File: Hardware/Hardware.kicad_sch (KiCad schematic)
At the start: 0 parts

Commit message: feat: add symbols, footprints and 3d models
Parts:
- added U1: ESP32-C3_SUPERMINI_TH, footprints:MODULE_ESP32-C3_SUPERMINI_TH, symbol ESP32-C3_SUPERMINI_TH:ESP32-C3_SUPERMINI_TH
- added U2: DM-OLED096-636, DM-OLED096-636:MODULE_DM-OLED096-636, symbol DM-OLED096-636:DM-OLED096-636

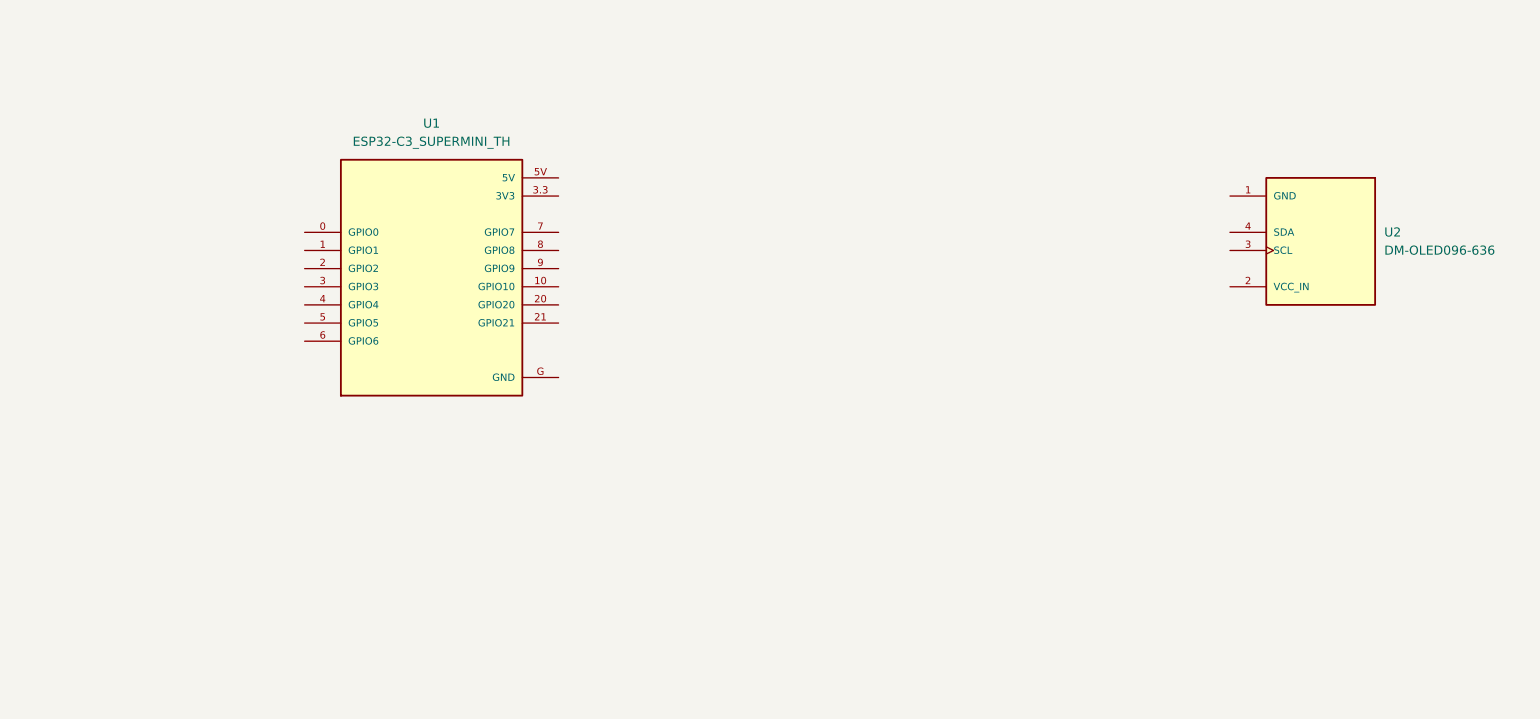
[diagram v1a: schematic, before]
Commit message: feat: add schematic design
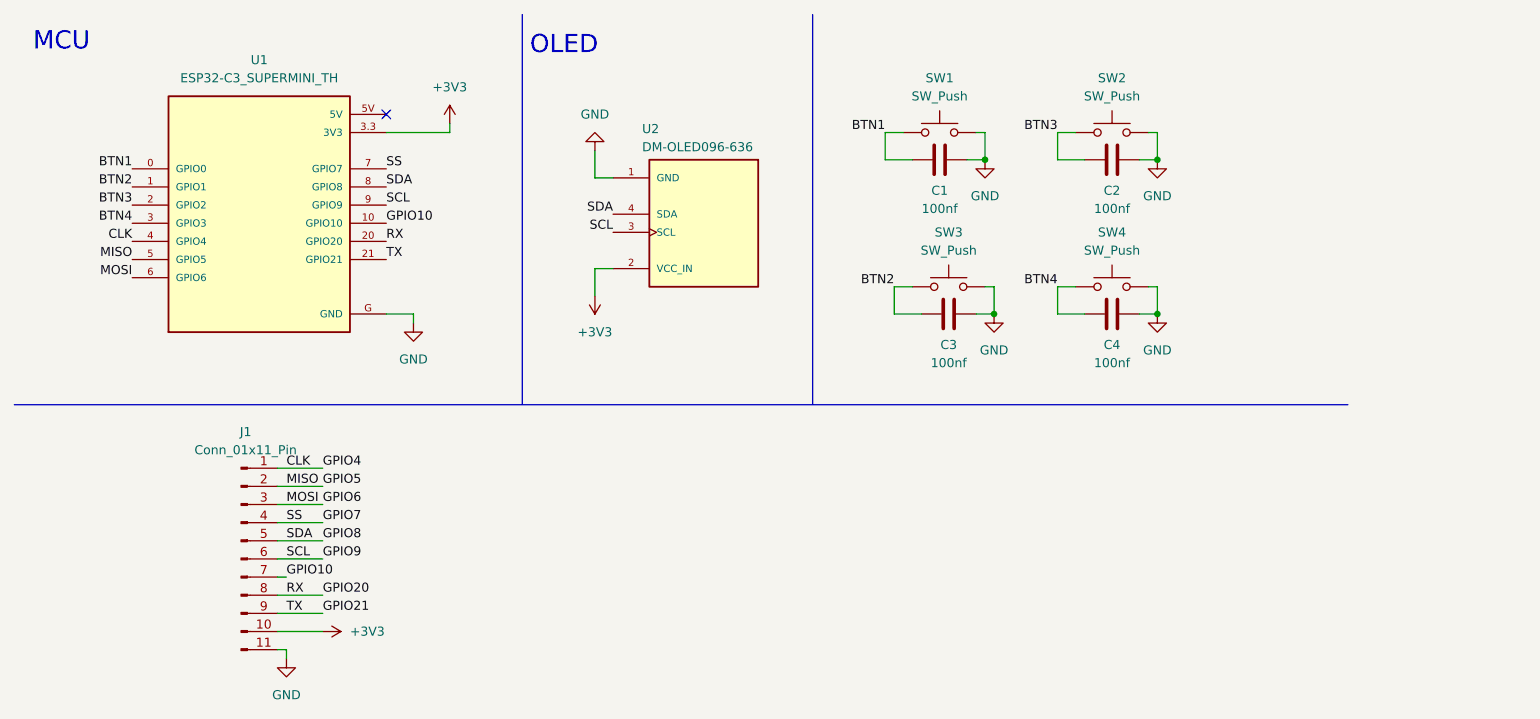
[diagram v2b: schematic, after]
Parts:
- added C1, C2, C3, C4: 100nf, symbol Device:C
- added J1: Conn_01x11_Pin, symbol Connector:Conn_01x11_Pin
- added SW1, SW2, SW3, SW4: SW_Push, symbol Switch:SW_Push
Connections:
- net BTN1: now reaches U1.0 (GPIO0)
- net BTN1: now also C1.1, SW1.1
- net BTN2: now reaches U1.1 (GPIO1)
- net BTN2: now also C3.1, SW3.1
- net GPIO10: now reaches U1.10 (GPIO10)
- net GPIO10: now also J1.7 (Pin_7)
- net BTN3: now reaches U1.2 (GPIO2)
- net BTN3: now also C2.1, SW2.1
- net GPIO20: now reaches U1.20 (GPIO20)
- net GPIO20: now also J1.8 (Pin_8)
- net GPIO21: now reaches U1.21 (GPIO21)
- net GPIO21: now also J1.9 (Pin_9)
- net BTN4: now reaches U1.3 (GPIO3)
- net BTN4: now also C4.1, SW4.1
- net +3V3: now reaches U1.3.3 (3V3)
- net +3V3: now also U2.2 (VCC_IN), J1.10 (Pin_10)
- net CLK: now reaches U1.4 (GPIO4)
- net CLK: now also J1.1 (Pin_1)
- net GPIO5: now reaches U1.5 (GPIO5)
- net GPIO5: now also J1.2 (Pin_2)
- net GPIO6: now reaches U1.6 (GPIO6)
- net GPIO6: now also J1.3 (Pin_3)
- net GPIO7: now reaches U1.7 (GPIO7)
- net GPIO7: now also J1.4 (Pin_4)
- net GPIO8: now reaches U1.8 (GPIO8)
- net GPIO8: now also U2.4 (SDA), J1.5 (Pin_5)
- net GPIO9: now reaches U1.9 (GPIO9)
- net GPIO9: now also U2.3 (SCL), J1.6 (Pin_6)
- net GND: now reaches U1.G (GND)
- net GND: now also U2.1 (GND), C1.2, C2.2, C3.2, C4.2, J1.11 (Pin_11), SW1.2, SW2.2, SW3.2, SW4.2
- no-connect marks 0 -> 1
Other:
- note added: "MCU"
- note added: "OLED"
- title: (none) -> My Esp32c3 
- moved on the sheet: U1, U2

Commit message: feat: change esp model & add footprints
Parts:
- J1: footprint (none) -> Connector_PinHeader_2.54mm:PinHeader_1x11_P2.54mm_Vertical
- SW1, SW2, SW3, SW4: footprint (none) -> Button_Switch_THT:SW_PUSH_6mm
- U1: footprint footprints:MODULE_ESP32-C3_SUPERMINI_TH -> footprints:MODULE_ESP32-C3_SUPERMINI
- U2: footprint DM-OLED096-636:MODULE_DM-OLED096-636 -> footprints:MODULE_DM-OLED096-636
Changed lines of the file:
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@@
 			)
 		)
-		(property "Footprint" ""
+		(property "Footprint" "Connector_PinHeader_2.54mm:PinHeader_1x11_P2.54mm_Vertical"
 			(at 43.18 87.63 0)
 			(effects
@@
 			)
 		)
-		(property "Footprint" ""
+		(property "Footprint" "Button_Switch_THT:SW_PUSH_6mm"
 			(at 140.97 22.86 0)
 			(effects
@@
 			)
 		)
-		(property "Footprint" "footprints:MODULE_ESP32-C3_SUPERMINI_TH"
+		(property "Footprint" "footprints:MODULE_ESP32-C3_SUPERMINI"
 			(at 45.72 38.1 0)
 			(effects
@@
 			)
 		)
-		(property "Footprint" ""
+		(property "Footprint" "Button_Switch_THT:SW_PUSH_6mm"
 			(at 165.1 44.45 0)
 			(effects
@@
 			)
 		)
-		(property "Footprint" ""
+		(property "Footprint" "Button_Switch_THT:SW_PUSH_6mm"
 			(at 142.24 44.45 0)
 			(effects
@@
 			)
 		)
-		(property "Footprint" "DM-OLED096-636:MODULE_DM-OLED096-636"
+		(property "Footprint" "footprints:MODULE_DM-OLED096-636"
 			(at 107.95 39.37 0)
 			(effects
@@
 			)
 		)
-		(property "Footprint" ""
+		(property "Footprint" "Button_Switch_THT:SW_PUSH_6mm"
 			(at 165.1 22.86 0)
 			(effects

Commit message: feat: add routes
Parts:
- removed J1: Conn_01x11_Pin, Connector_PinHeader_2.54mm:PinHeader_1x11_P2.54mm_Vertical, symbol Connector:Conn_01x11_Pin
- removed SW1, SW2, SW3, SW4: SW_Push, Button_Switch_THT:SW_PUSH_6mm, symbol Switch:SW_Push
- added C5: 100nF, Capacitor_SMD:C_0603_1608Metric_Pad1.08x0.95mm_HandSolder, symbol Device:C
- added J1: Conn_01x10_Socket, Connector_PinHeader_2.54mm:PinHeader_1x10_P2.54mm_Vertical, symbol Connector:Conn_01x10_Socket
- added S1: JS1400AFQ, footprints:SW_JS1400AFQ, symbol JS1400AFQ:JS1400AFQ
- C1, C2, C3, C4: value 100nf -> 100nF; footprint (none) -> Capacitor_SMD:C_0603_1608Metric_Pad1.08x0.95mm_HandSolder
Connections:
- net +3V3: now also J1.9 (Pin_9)
- net CLK: now also J1.1 (Pin_1)
- net GND: now also C5.2, J1.10 (Pin_10), S1.5, S1.G1 (GND), S1.G2 (GND)
- net BTN1 renamed F1
- net F1: now also C2.1, S1.3; no longer C1.1
- net BTN2 renamed F2
- net F2: now also C1.1, S1.1; no longer C3.1
- net BTN3 renamed F4
- net F4: now also C5.1, S1.2; no longer C2.1
- net BTN4 renamed F3
- net F3: now also S1.6
- net GPIO10 renamed F5
- net F5: now also C3.1, S1.4
- net GPIO20 renamed RX
- net RX: now also J1.8 (Pin_8)
- net GPIO21 renamed TX
- net TX: now also J1.7 (Pin_7)
- net GPIO5 renamed MISO
- net MISO: now also J1.2 (Pin_2)
- net GPIO6 renamed MOSI
- net MOSI: now also J1.3 (Pin_3)
- net GPIO7 renamed SS
- net SS: now also J1.4 (Pin_4)
- net GPIO8 renamed SDA
- net SDA: now also J1.5 (Pin_5)
- net GPIO9 renamed SCL
- net SCL: now also J1.6 (Pin_6)
